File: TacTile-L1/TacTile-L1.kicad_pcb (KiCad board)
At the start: 2 copper layers, 2 parts, among them J1 Conn_01x02, J2 Conn_01x02

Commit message: Finished L1 Board
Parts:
- added LD1: D_Laser_1C2A, TacTile:Laser_Diode, F.Cu at (39.0, 28.8)
- added LD2: D_Laser_1C2A, TacTile:Laser_Diode, F.Cu at (39.0, 36.2)
- added LD3: D_Laser_1C2A, TacTile:Laser_Diode, F.Cu at (39.0, 43.8)
- added LD4: D_Laser_1C2A, TacTile:Laser_Diode, F.Cu at (39.0, 51.2)
- added LD5: D_Laser_1C2A, TacTile:Laser_Diode, F.Cu at (39.0, 58.8)
- added LD6: D_Laser_1C2A, TacTile:Laser_Diode, F.Cu at (39.0, 66.2)
- added LD7: D_Laser_1C2A, TacTile:Laser_Diode, F.Cu at (39.0, 73.8)
- added LD8: D_Laser_1C2A, TacTile:Laser_Diode, F.Cu at (39.0, 81.2)
- J1, J2: moved to B.Cu
- moved J1 51.4 mm to (31.5, 81.9), turned to -90 degrees
- moved J2 9.96 mm to (31.5, 32.7), turned to -90 degrees
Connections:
- J1 pad 1: Net-(J1-Pin_1) -> /VCC
- J1 pad 2: Net-(J1-Pin_2) -> /GND
- J2 pad 1: Net-(J1-Pin_2) -> /VCC
- J2 pad 2: Net-(J1-Pin_1) -> /GND
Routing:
- added copper zone on B.Cu, net /GND
- added copper zone on F.Cu, net /VCC
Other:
- board outline added: 18.2 x 60 mm

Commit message: Finished enlarging pins on C, D, L1, L2
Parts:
- J1: footprint Connector_PinHeader_2.00mm:PinHeader_1x02_P2.00mm_Horizontal -> Connector_PinSocket_2.54mm:PinSocket_1x02_P2.54mm_Horizontal
- J2: footprint Connector_PinSocket_2.00mm:PinSocket_1x02_P2.00mm_Horizontal -> Connector_PinHeader_2.54mm:PinHeader_1x02_P2.54mm_Horizontal
- moved J1 7.28 mm to (33.5, 74.9), turned to 90 degrees
- moved J2 4.12 mm to (33.5, 29.1), turned to 90 degrees
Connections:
- J1 pad 1: /VCC -> /GND
- J1 pad 2: /GND -> /VCC
- J2 pad 1: /VCC -> /GND
- J2 pad 2: /GND -> /VCC
- LD1 pad 1: /VCC -> /GND
- LD1 pad 2: /GND -> /VCC
- LD2 pad 1: /VCC -> /GND
- LD2 pad 2: /GND -> /VCC
- LD3 pad 1: /VCC -> /GND
- LD3 pad 2: /GND -> /VCC
- LD4 pad 1: /VCC -> /GND
- LD4 pad 2: /GND -> /VCC
- LD5 pad 1: /VCC -> /GND
- LD5 pad 2: /GND -> /VCC
- LD6 pad 1: /VCC -> /GND
- LD6 pad 2: /GND -> /VCC
- LD7 pad 1: /VCC -> /GND
- LD7 pad 2: /GND -> /VCC
- LD8 pad 1: /VCC -> /GND
- LD8 pad 2: /GND -> /VCC

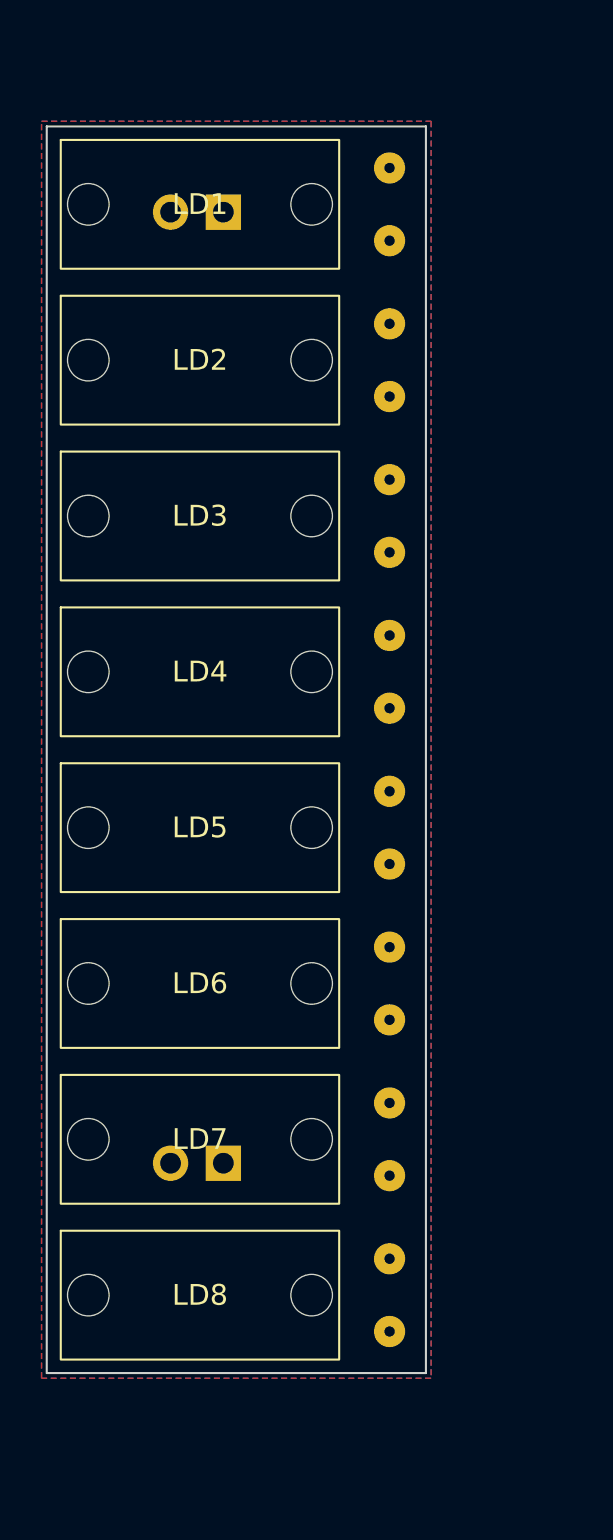
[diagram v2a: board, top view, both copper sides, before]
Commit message: Created connector boards for laser matrix
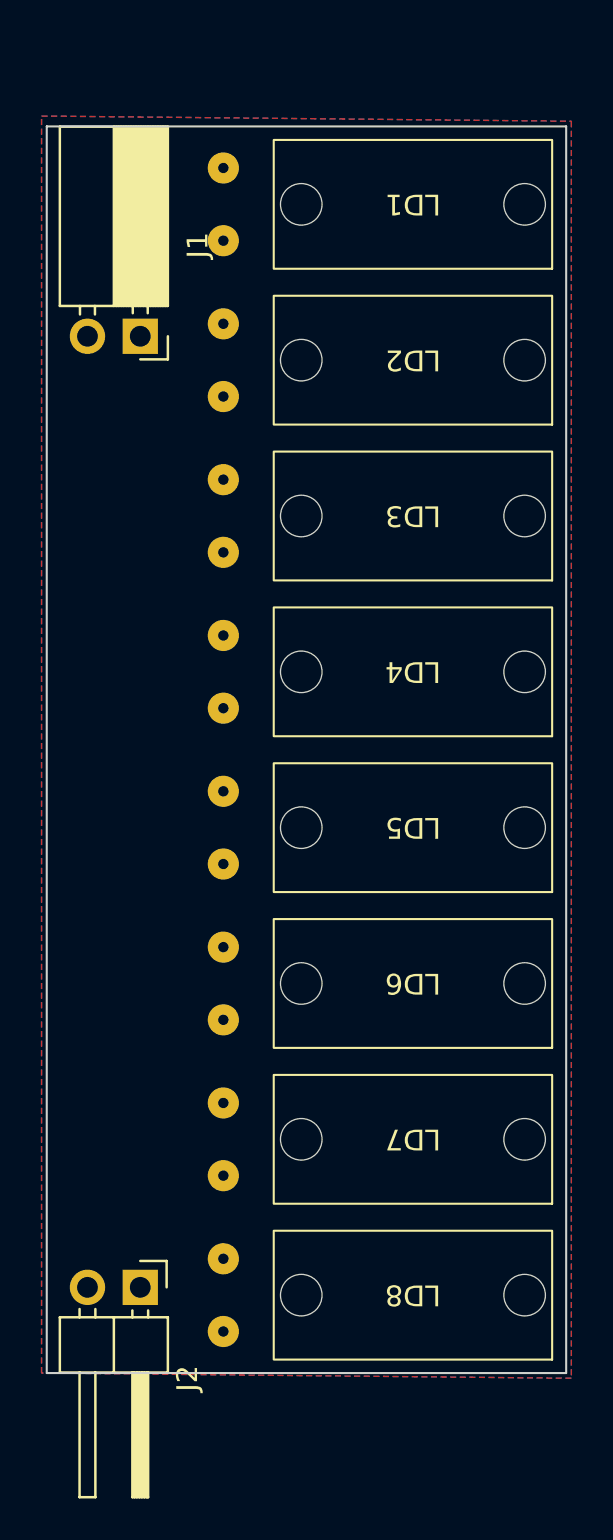
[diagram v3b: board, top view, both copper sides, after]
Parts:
- J1, J2: moved to F.Cu
- moved J2 51.9 mm to (29.5, 80.9), turned to -90 degrees
- moved J1 40.0 mm to (29.5, 35.1), turned to -90 degrees
- moved LD1 3.00 mm to (36.0, 28.8), turned to 180 degrees
- moved LD2 3.00 mm to (36.0, 36.2), turned to 180 degrees
- moved LD3 3.00 mm to (36.0, 43.8), turned to 180 degrees
- moved LD4 3.00 mm to (36.0, 51.2), turned to 180 degrees
- moved LD5 3.00 mm to (36.0, 58.8), turned to 180 degrees
- moved LD6 3.00 mm to (36.0, 66.2), turned to 180 degrees
- moved LD7 3.00 mm to (36.0, 73.8), turned to 180 degrees
- moved LD8 3.00 mm to (36.0, 81.2), turned to 180 degrees
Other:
- board size 18.2 x 60 mm -> 25 x 60 mm
